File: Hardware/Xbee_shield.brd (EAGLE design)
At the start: 53.3 x 59.7 mm, 39 parts, among them Q1 MOSFET-NCHANNELSMD, Q2 MOSFET-NCHANNELSMD, U1 ARDUINO_SHIELD, U2 XBEE-1B3, U4 V_REG_LDOSMD

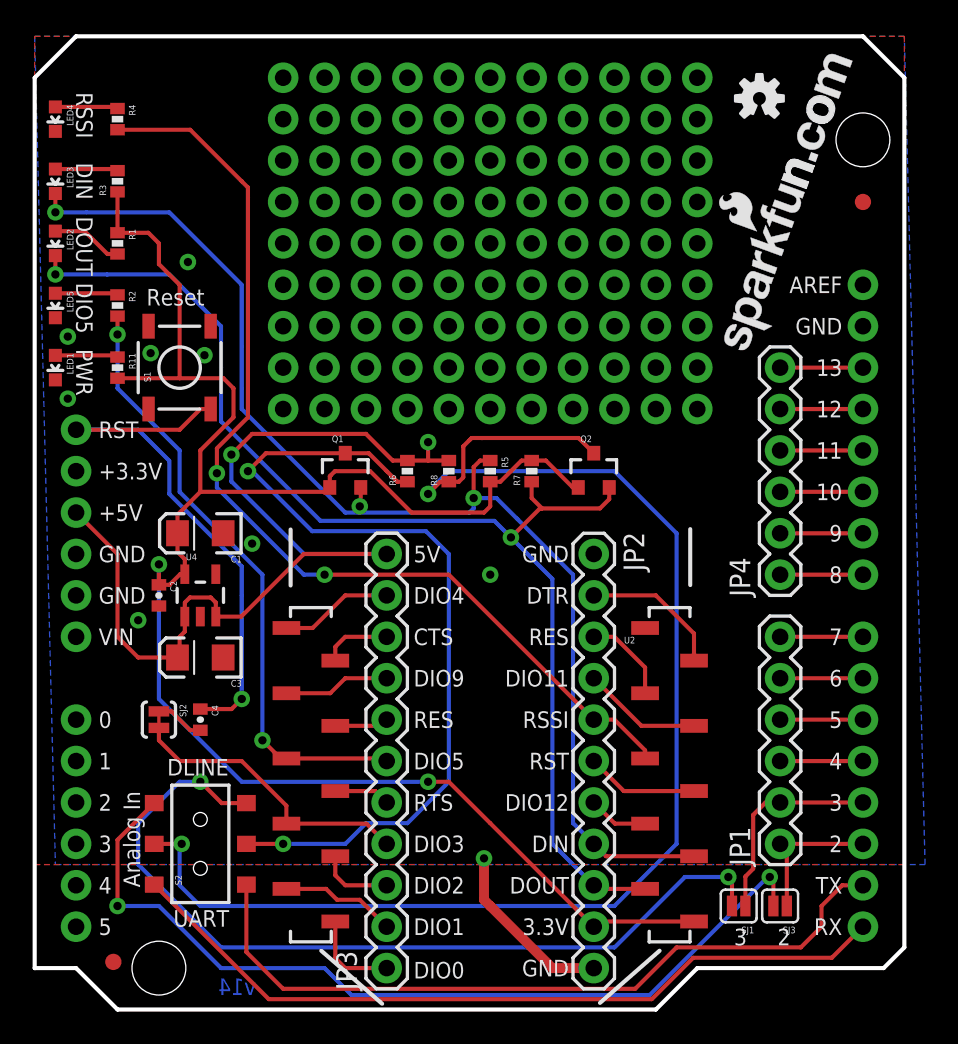
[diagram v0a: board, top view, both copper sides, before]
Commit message: Updates to res/caps/r3 sheild, trace re routes
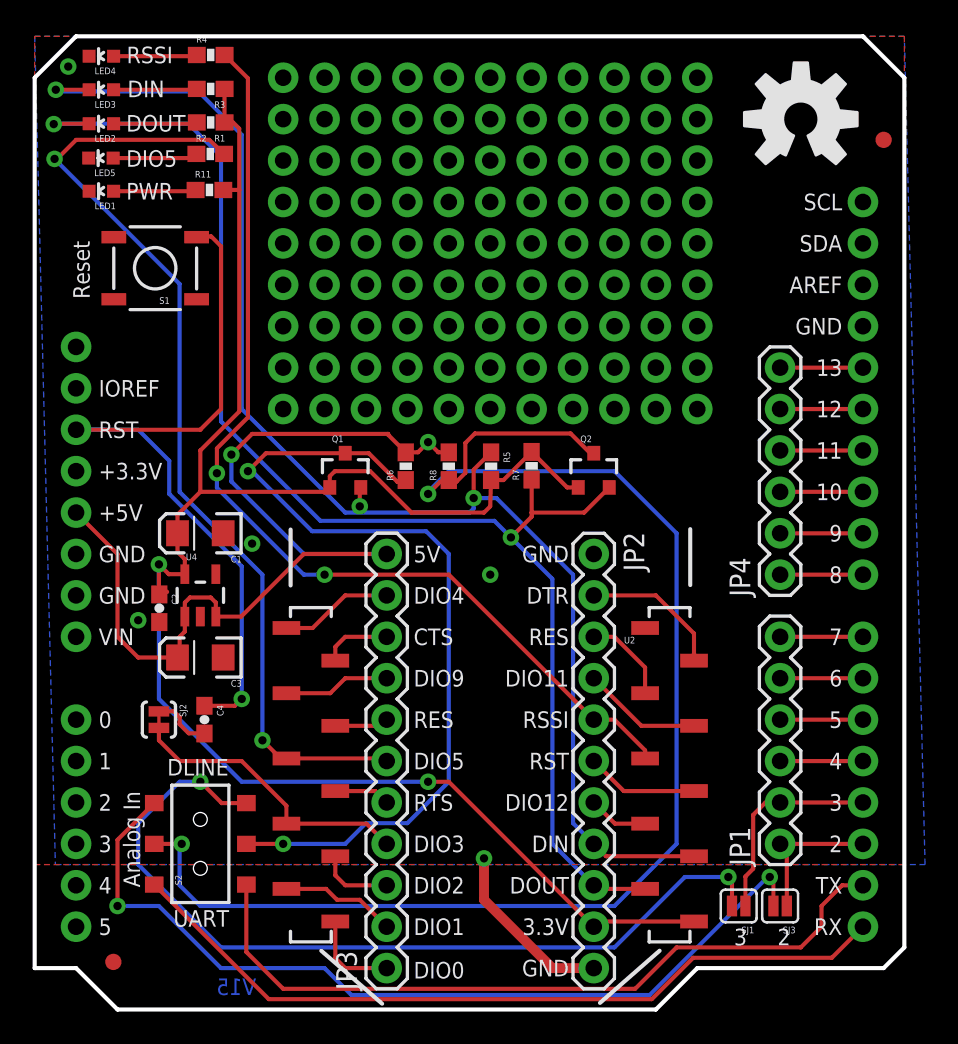
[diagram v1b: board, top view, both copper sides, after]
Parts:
- removed U$4: LOGO-SFENEW, SparkFun:SFE-NEW-WEBLOGO
- C2, C4: device SparkFun:0402-CAP -> SparkFun-Capacitors:0603-CAP
- R1, R11, R2, R3, R4, R5, R6, R7, R8: device SparkFun:0402-RES -> SparkFun-Resistors:0603-RES
- U$8: value OSHW-LOGOS -> OSHW-LOGOL; device SparkFun-Aesthetics:OSHW-LOGO-S -> SparkFun-Aesthetics:OSHW-LOGO-L
- U1: device SparkFun:DUEMILANOVE_SHIELD -> SparkFun-Boards:UNO_R3_SHIELD
- moved R11 12.3 mm to (10.7, 50.3), turned to 0 degrees
- moved LED1 11.2 mm to (4.09, 50.2), turned to 90 degrees
- moved R2 10.9 mm to (10.8, 52.5), turned to 0 degrees
- moved LED5 9.46 mm to (4.06, 52.2), turned to 90 degrees
- moved R1 9.36 mm to (10.8, 54.4), turned to 180 degrees
- moved R3 8.05 mm to (10.8, 56.5), turned to 180 degrees
- moved LED2 7.86 mm to (4.09, 54.3), turned to 90 degrees
- moved R4 6.94 mm to (10.8, 58.5), turned to 0 degrees
- moved LED3 6.28 mm to (4.09, 56.4), turned to 90 degrees
- moved S1 6.28 mm to (7.39, 45.5), turned to 180 degrees
- moved LED4 4.78 mm to (4.09, 58.5), turned to 90 degrees
- moved JP6 4.02 mm to (52.1, 53.3)
- moved U$8 2.84 mm to (47.0, 54.6)
- moved C2 0.79 mm to (7.65, 24.6)
- moved R7 0.33 mm to (30.5, 33.4)
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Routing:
- net DIO5: track 37.8 -> 60.3 mm
- net RST: track 36.3 -> 48.3 mm
- net DOUT: track 75.5 -> 86.4 mm
- net DIN: track 75.8 -> 85.4 mm
- net N$4: track 3.85 -> 5.86 mm
- net N$2: track 3.85 -> 5.77 mm
- net N$139: track 3.85 -> 5.71 mm
- net N$38: track 3.85 -> 5.69 mm
- net N$1: track 4.39 -> 5.82 mm
- net 5V: track 60.2 -> 59.4 mm
- net RSSI: track 62.1 -> 61.4 mm
- net N$5: track 3.02 -> 3.61 mm
- net GND: vias 9 -> 5
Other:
- board text added: "V15"
- board text removed: "v14"

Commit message: Fixed LED's/Silk
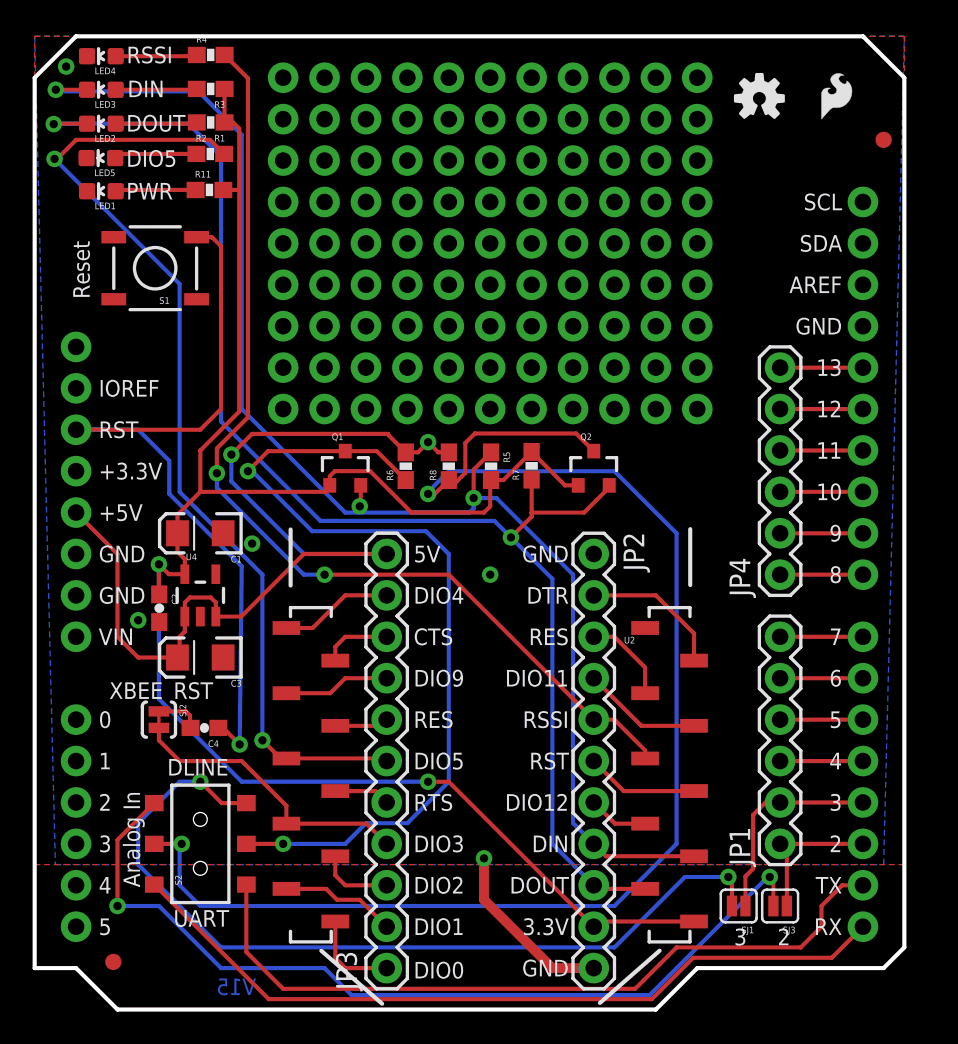
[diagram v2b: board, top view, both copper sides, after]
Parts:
- added U$4: (no value), SparkFun-Aesthetics:SFE-LOGO-FLAME
- LED1, LED2, LED3, LED4, LED5: device SparkFun:LED-0603 -> SparkFun-LED:LED-0603
- U$8: value OSHW-LOGOL -> OSHW-LOGOS; device SparkFun-Aesthetics:OSHW-LOGO-L -> SparkFun-Aesthetics:OSHW-LOGO-S
- moved U$8 2.84 mm to (44.5, 55.9)
- moved C4 0.51 mm to (10.4, 17.3), turned to 180 degrees
- moved Q1 0.13 mm to (19.1, 33.1)
- moved Q2 0.13 mm to (34.3, 33.1)
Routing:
- net RST: track 48.3 -> 50.4 mm
- net N$4: track 5.86 -> 5.00 mm
- net N$5: track 3.61 -> 2.79 mm
- net N$1: track 5.82 -> 5.01 mm
- net N$38: track 5.69 -> 4.93 mm
- net N$2: track 5.77 -> 5.01 mm
- net N$139: track 5.71 -> 5.08 mm
- net 3.3V: track 112.9 -> 112.3 mm
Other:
- board text added: "XBEE"

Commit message: Sch work
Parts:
- removed U$4: (no value), SparkFun-Aesthetics:SFE-LOGO-FLAME
- removed U$5: CREATIVE_COMMONS, SparkFun:CREATIVE_COMMONS
- added FRAME1: FRAME-LETTER, SparkFun-Aesthetics:CREATIVE_COMMONS
- U$1: value LOGO-SFESK -> (none); device SparkFun:SFE-LOGO-FLAME -> SparkFun-Aesthetics:SFE_LOGO_FLAME_.3
- moved U$8 39.9 mm to (7.62, 40.6)
- moved U$1 32.0 mm to (43.9, 51.3), flipped to the top
- moved JP7 6.87 mm to (36.4, 28.4), turned to 0 degrees
- moved JP6 1.27 mm to (50.8, 53.3)
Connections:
- net N$67: now also U1.SCL, U1.SDA
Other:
- board text added: "A. Weiss"
- board text added: "Revised by: Patrick Alberts"
- board text added: "Xbee Sheild"

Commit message: Changes to Silk/SCH
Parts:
- JP4: device SparkFun:1X06 -> SparkFun-Connectors:1X10
- U$1: device SparkFun-Aesthetics:SFE_LOGO_FLAME_.3 -> SparkFun-Aesthetics:SFE_LOGO_FLAME_.2
- moved FRAME1 87.9 mm to (-2.01, -16.5)
- moved JP7 16.9 mm to (27.2, 14.4), turned to 90 degrees
- moved U$1 1.53 mm to (44.6, 52.7)
- moved JP4 1.52 mm to (44.2, 26.7)
- moved JP1 1.40 mm to (44.3, 10.2)
- moved R2 0.56 mm to (10.8, 51.9)
- moved LED1 0.50 mm to (3.89, 49.7)
- moved LED4 0.45 mm to (3.89, 58.1)
- moved LED3 0.44 mm to (3.86, 56.0)
- moved LED2 0.43 mm to (3.89, 53.9)
- moved LED5 0.43 mm to (3.86, 51.8)
- moved R1 0.38 mm to (10.8, 54.0)
- moved R11 0.38 mm to (10.7, 49.9)
- moved R3 0.38 mm to (10.8, 56.1)
- moved R4 0.38 mm to (10.8, 58.2)
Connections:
- removed net N$67: JP4.6, U1.D13, U1.SCL, U1.SDA
- new net AREF: JP4.8, U1.AREF
- new net N$3: JP4.6, U1.D13
- new net N$6: JP4.9, U1.SDA
- new net N$7: JP4.10, U1.SCL
- net GND: now also JP4.7
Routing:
- net N$7: track 0.00 -> 6.60 mm
- net N$6: track 0.00 -> 6.60 mm
- net N$3: track 0.00 -> 6.60 mm
- net AREF: track 0.00 -> 6.60 mm
- net N$67: track 5.08 -> 0.00 mm
- net D_RX: track 9.06 -> 11.0 mm
- net D_TX: track 12.8 -> 14.4 mm
- net N$55: track 5.08 -> 6.60 mm
- net N$43: track 5.08 -> 6.60 mm
- net N$30: track 5.08 -> 6.60 mm
- net N$18: track 5.08 -> 6.60 mm
- net N$17: track 5.08 -> 6.60 mm
- net N$145: track 5.08 -> 6.48 mm
- net N$144: track 5.08 -> 6.48 mm
- net N$143: track 5.08 -> 6.48 mm
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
